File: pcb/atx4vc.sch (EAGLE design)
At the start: 69 parts, among them IC2 REG1117, IC3 STM32F042F4, IC4 MY_7905DT, J1 ATX24RH, SW1 324_SW, SW2 324_SW, SW3 324_SW, SW4 324_SW, SW5 324_SW, SW7 324_SW, U1 USBC_16P, U2 USBC_16P

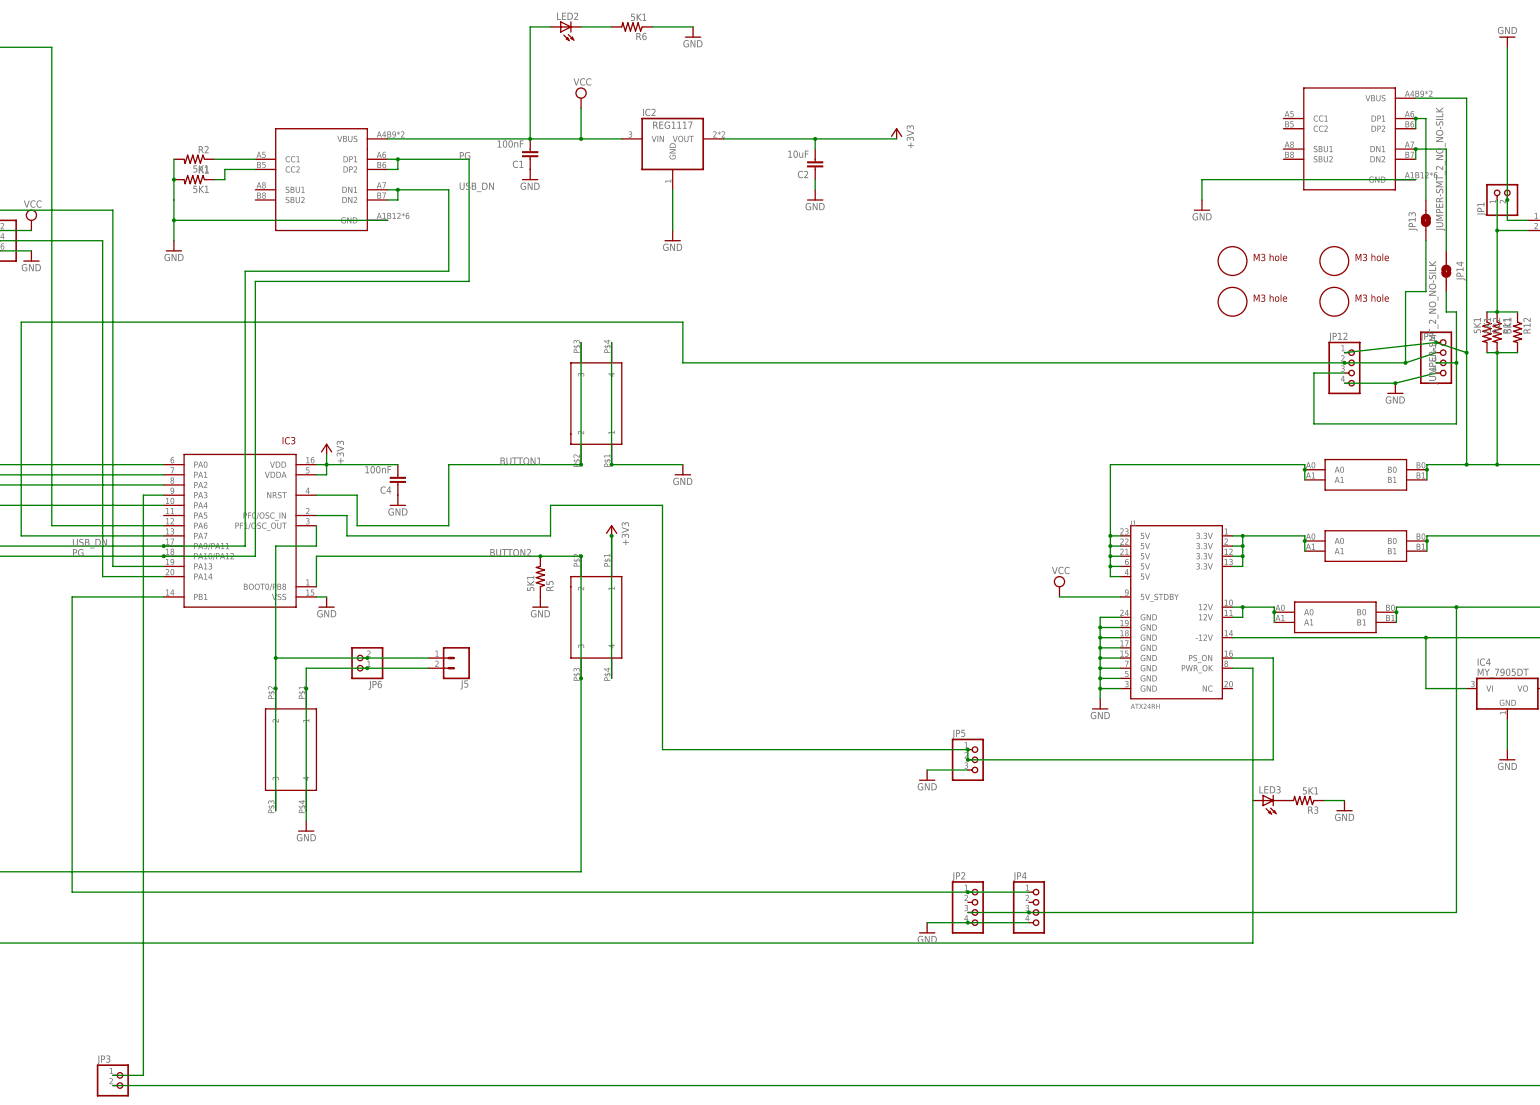
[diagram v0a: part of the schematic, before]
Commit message: adjusted ARGB header
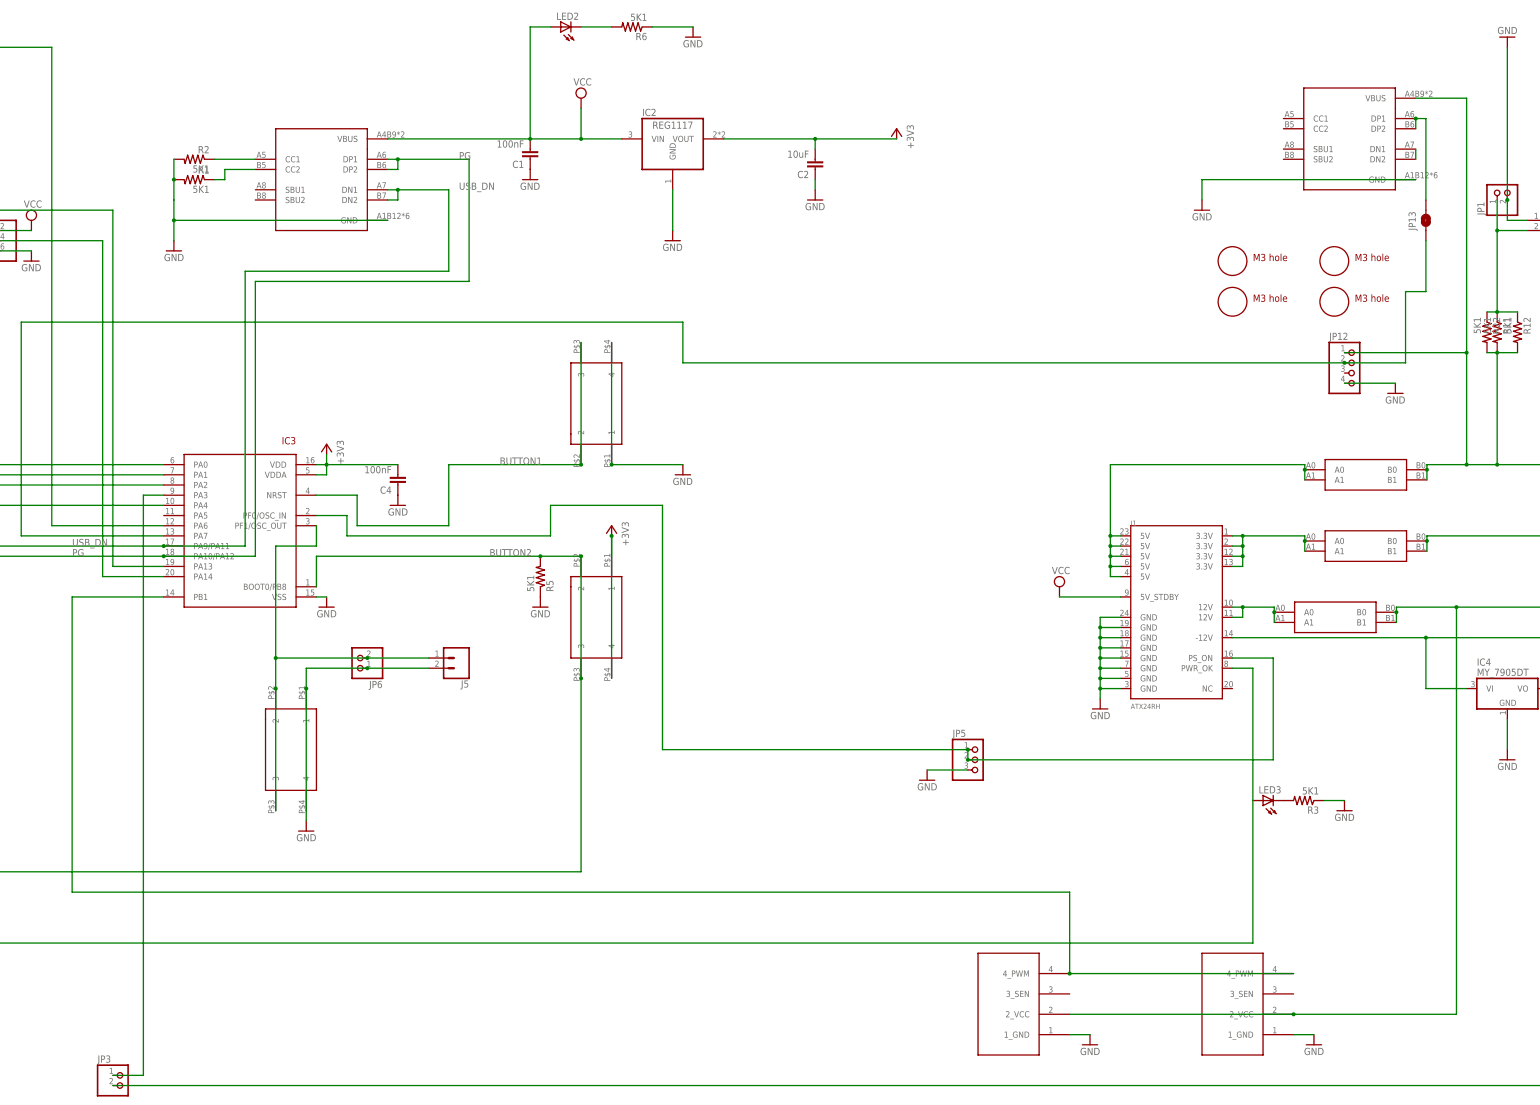
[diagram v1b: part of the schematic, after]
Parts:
- removed JP14: JUMPER-SMT_2_NO_NO-SILK, SparkFun-Jumpers:JUMPER-SMT_2_NO_NO-SILK
- removed JP2, JP4: (no value), atx_power_control:PINHD-1X4
- removed JP7: (no value), atx_power_control:PINHD-1X6
- added JP16, JP8: (no value), appleii:4PIN_FAN
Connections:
- removed net N$37: JP12.3, JP14.2, JP7.3
- net F12V: now also JP16.2_VCC, JP8.2_VCC; no longer JP2.3, JP4.3
- net F5V: no longer JP7.1
- net GND: now also JP16.1_GND, JP8.1_GND; no longer JP2.4, JP4.4, JP7.4
- net N$35: no longer JP7.2
- net N$36: no longer JP14.1
- net N$7: now also JP16.4_PWM, JP8.4_PWM; no longer JP2.1, JP4.1

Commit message: finishing touches
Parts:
- JP11: device atx_power_control:PINHD-1X3CB -> pinhead:PINHD-1X3
- JP12: device atx_power_control:PINHD-1X6 -> pinhead:PINHD-1X4
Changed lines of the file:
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@@
 <part name="U$7" library="atx_power_control" deviceset="CAR_FUSE_HOLDER" device="3IN1"/>
 <part name="U$8" library="atx_power_control" deviceset="CAR_FUSE_HOLDER" device="3IN1"/>
-<part name="JP12" library="atx_power_control" deviceset="PINHD-1X6" device=""/>
+<part name="JP12" library="pinhead" library_urn="urn:adsk.eagle:library:325" deviceset="PINHD-1X4" device="" package3d_urn="urn:adsk.eagle:package:22407/2"/>
 <part name="R14" library="atx_power_control" deviceset="RESISTOR" device="0805-RES" value="5K1"/>
-<part name="JP11" library="atx_power_control" deviceset="PINHD-1X3" device="CB"/>
+<part name="JP11" library="pinhead" library_urn="urn:adsk.eagle:library:325" deviceset="PINHD-1X3" device="" package3d_urn="urn:adsk.eagle:package:22458/2"/>
 <part name="SUPPLY1" library="supply2" library_urn="urn:adsk.eagle:library:372" deviceset="VCC" device=""/>
 <part name="GND34" library="supply1" deviceset="GND" device=""/>
@@
 <instance part="U$7" gate="G$1" x="281.94" y="20.32" smashed="yes"/>
 <instance part="U$8" gate="G$1" x="281.94" y="38.1" smashed="yes"/>
-<instance part="JP12" gate="A" x="279.4" y="60.96" smashed="yes">
-<attribute name="NAME" x="273.05" y="71.755" size="1.778" layer="95"/>
-<attribute name="VALUE" x="273.05" y="50.8" size="1.778" layer="96"/>
+<instance part="JP12" gate="A" x="279.4" y="63.5" smashed="yes">
+<attribute name="NAME" x="273.05" y="74.295" size="1.778" layer="95"/>
+<attribute name="VALUE" x="273.05" y="53.34" size="1.778" layer="96"/>
 </instance>
 <instance part="R14" gate="G$1" x="-86.36" y="149.86" smashed="yes" rot="R90">

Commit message: added 5VSB to terminal block, cleaned up files
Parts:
- removed C1, C4: 100nF, atx_power_control:CAP0805
- removed C2: 10uF, atx_power_control:CAP0805
- removed IC2: REG1117, atx_power_control:REG1117
- removed IC3: STM32F042F4, tx:STM32F042F4
- removed J5, J8: (no value), atx_power_control:CONN_023.5MM
- removed JP10: (no value), adafruit:PINHD-1X1CB
- removed JP11: (no value), pinhead:PINHD-1X3
- removed JP12: (no value), pinhead:PINHD-1X4
- removed JP13: JUMPER-SMT_2_NO_NO-SILK, SparkFun-Jumpers:JUMPER-SMT_2_NO_NO-SILK
- removed JP15: (no value), pinhead:PINHD-2X3
- removed JP16: (no value), appleii:4PIN_FAN
- removed JP5: (no value), atx_power_control:PINHD-1X3:1
- removed JP6: (no value), atx_power_control:PINHD-1X2
- removed JP9: (no value), atx_power_control:PINHD-2X4
- removed LED8: (no value), adafruit:LEDCHIP-LED0805
- removed R1, R14, R15, R18, R19, R2, R20, R21, R5: 5K1, atx_power_control:RESISTOR0805-RES
- removed SW1, SW2, SW3, SW4, SW5, SW7: 324_SW, 3pos_slide_switch_centered:324_SW
- removed U1, U2: USBC_16P, my_usbc_16p:USBC_16P
- added J4: (no value), SparkFun-Connectors:USB_C16PIN
- added JP2: (no value), pinhead:PINHD-1X2
- added JP4: (no value), pinhead:PINHD-2X2
- added U$11: M3_MOUNTING_HOLE, a:M3_MOUNTING_HOLE
- added U$12: PINHD1X4, adafruit_changed:PINHD1X4
- J1: device SparkFun-Connectors:ATX24RH -> nomcu:ATX24RH
- JP3: device pinhead:PINHD-1X2 -> pinhead:PINHD-2X3
- U$6: value 74LVC2G08 -> M3_MOUNTING_HOLE; device atx4vc:74LVC2G08 -> a:M3_MOUNTING_HOLE
- U$9: value WAGO257-7 -> DG2204R-5.0; device atx4vc:WAGO257-7 -> atx4vc:DG2204R-5.0
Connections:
- removed net +3V3: C2.2, C4.2, IC2.VOUT, IC3.VDD, IC3.VDDA, JP15.5, JP9.4, SW4.1, SW4.4, U$6.8_VCC
- removed net BUTTON1: IC3.NRST, SW3.2, SW3.3
- removed net BUTTON2: IC3.BOOT0/PB8, JP9.3, R5.2, SW4.2, SW4.3
- removed net F12V_DIV2: R18.2, R19.1, U$6.6_2B
- removed net N$12: U$6.2_1B, U$6.3_2Y
- removed net N$13: IC3.PA0, JP9.6, SW2.1, SW2.4
- removed net N$19: LED8.A, R15.2
- removed net N$22: IC3.PA1, JP9.8, SW5.1, SW5.4
- removed net N$23: IC3.PA2, JP10.1
- removed net N$24: JP3.2, U$6.7_1Y
- removed net N$25: IC3.PF0/OSC_IN, J1.PS_ON, JP5.1, JP5.2
- removed net N$26: IC3.PF1/OSC_OUT, J5.1, JP6.2, SW1.2, SW1.3
- removed net N$27: IC3.PA4, JP9.2, SW7.1, SW7.4
- removed net N$31: R1.1, U2.CC2
- removed net N$33: R2.1, U2.CC1
- removed net N$34: JP13.2, U1.DP1, U1.DP2
- removed net N$35: IC3.PA7, JP12.2, JP13.1
- removed net N$36: U1.DN1, U1.DN2
- removed net N$38: IC3.PA3, JP3.1
- removed net PG: IC3.PA10/PA12, J1.PWR_OK, JP15.1, LED3.A, U2.DP1, U2.DP2
- removed net USB_DN: IC3.PA9/PA11, R15.1, U2.DN1, U2.DN2
- new net N$11: J1.PWR_OK, JP3.5, LED3.A
- new net N$15: J1.PS_ON, JP2.2, JP3.6
- net -12V: now also U$9.P$7; no longer U$9.P$1
- net -5V: now also U$9.P$6; no longer U$9.P$2
- net F12V: now also U$4.P$5, U$9.P$3; no longer JP16.2_VCC, R18.1, U$4.P$7, U$9.P$7
- net F3V3: now also U$9.P$5; no longer R21.2, U$6.1_1A, U$9.P$3
- net F5V: now also J4.VBUS, U$12.1, U$4.P$4, U$9.P$4; no longer JP12.1, R20.1, U$4.P$5, U$6.5_2A, U$9.P$5, U1.VBUS
- net GND: now also J4.GND, J4.SHLD, JP2.1, JP3.2, U$12.4, U$9.P$2; no longer C1.1, C2.1, C4.1, IC2.GND, IC3.VSS, J5.2, J8.1, JP11.3, JP12.4, JP15.6, JP16.1_GND, JP5.3, JP6.1, JP9.1, JP9.5, JP9.7, LED8.C, R1.2, R19.2, R2.2, R20.2, R21.1, R5.1, SW1.1, SW1.4, SW2.2, SW2.3, SW3.1, SW3.4, SW5.2, SW5.3, SW7.2, SW7.3, U$4.P$4, U$6.4_GND, U$9.P$4, U$9.P$6, U1.GND, U2.GND
- net N$17: no longer J8.2
- net N$3: now also JP3.3, JP8.4_PWM; no longer IC3.PA14, JP15.4
- net N$4: now also J4.D+, JP4.2; no longer IC3.PA13, JP15.3
- net N$6: now also J4.D-, JP4.4; no longer IC3.PA6, JP11.1, R14.1
- net N$7: now also JP3.4, JP4.1, JP4.3, U$12.2; no longer IC3.PB1, JP16.4_PWM, JP8.4_PWM
- net VCC: now also JP3.1, U$4.P$7, U$9.P$1; no longer C1.2, IC2.VIN, JP11.2, JP15.2, R14.2, U2.VBUS
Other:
- moved on the sheet: R12

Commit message: finishing touches before production run
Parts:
- removed J4: (no value), SparkFun-Connectors:USB_C16PIN
- removed R11, R12: 5K1, atx_power_control:RESISTOR0805-RES
- added J2: ATX24RH, nomcu:ATX24RH
- added R1, R5: 5K1, atx_power_control:RESISTOR0805-RES
- C1: value 10uF -> 2.2uF
- J1: value ATX24RH -> (none); device nomcu:ATX24RH -> SparkFun-Connectors:USB_C16PIN
- JP1: device pinhead:PINHD-1X2 -> pinhead:PINHD-2X2
- JP4: device pinhead:PINHD-2X2 -> pinhead:PINHD-1X2
- R4, R7: device SparkFun-Passives:RESISTOR0805-RES -> atx_power_control:RESISTOR0805-RES
- R8, R9: device atx_power_control:RESISTOR0805-RES -> SparkFun-Passives:RESISTOR0805-RES
- U$10, U$11: value M3_MOUNTING_HOLE -> CAR_FUSE_HOLDER3IN1; device a:M3_MOUNTING_HOLE -> atx_power_control:CAR_FUSE_HOLDER3IN1
- U$12: value PINHD1X4 -> DG2204R-5.0; device adafruit_changed:PINHD1X4 -> atx4vc:DG2204R-5.0
- U$4: value VH396 -> M3_MOUNTING_HOLE; device 396_conn:VH396 -> a:M3_MOUNTING_HOLE
- U$5: value CAR_FUSE_HOLDER3IN1 -> M3_MOUNTING_HOLE; device atx_power_control:CAR_FUSE_HOLDER3IN1 -> a:M3_MOUNTING_HOLE
- U$7: value CAR_FUSE_HOLDER3IN1 -> VH396; device atx_power_control:CAR_FUSE_HOLDER3IN1 -> 396_conn:VH396
- U$8: value CAR_FUSE_HOLDER3IN1 -> PINHD1X4; device atx_power_control:CAR_FUSE_HOLDER3IN1 -> adafruit_changed:PINHD1X4
- U$9: value DG2204R-5.0 -> CAR_FUSE_HOLDER3IN1; device atx4vc:DG2204R-5.0 -> atx_power_control:CAR_FUSE_HOLDER3IN1
- renumbered C5 to C1, IC4 to IC1, JP8 to JP5, R22 to R2
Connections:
- removed net N$1 (its old number): LED3.C, R3.2
- removed net N$5 (its old number): LED1.C, R4.2
- new net N$18: LED3.C, R6.2
- new net N$20: LED2.C, R5.2
- net -12V: now also J2.-12V, R8.1, U$12.P$7, U$7.P$1; no longer J1.-12V, R7.1, U$4.P$1, U$9.P$7
- net -5V: now also R9.1, U$12.P$6, U$7.P$2; no longer R4.1, U$4.P$2, U$9.P$6
- net F12V: now also LED4.A, U$11.B0, U$11.B1, U$12.P$3, U$7.P$5; no longer LED5.A, U$4.P$5, U$5.B0, U$5.B1, U$9.P$3
- net F3V3: now also LED3.A, U$10.B0, U$10.B1, U$12.P$5, U$7.P$3; no longer LED6.A, U$4.P$3, U$7.B0, U$7.B1, U$9.P$5
- net F5V: now also J1.VBUS, LED2.A, R3.2, R4.2, U$12.P$4, U$7.P$4, U$8.1, U$9.B0, U$9.B1; no longer J4.VBUS, LED7.A, R11.2, R12.2, U$12.1, U$4.P$4, U$8.B0, U$8.B1, U$9.P$4
- net GND: now also J1.GND, J1.SHLD, J2.GND@0, J2.GND@1, J2.GND@2, J2.GND@3, J2.GND@4, J2.GND@5, J2.GND@6, J2.GND@7, JP2.2, JP4.1, LED5.A, LED6.A, R1.1, R5.1, R7.1, U$12.P$2, U$7.P$6, U$8.4; no longer J1.GND@0, J1.GND@1, J1.GND@2, J1.GND@3, J1.GND@4, J1.GND@5, J1.GND@6, J1.GND@7, J4.GND, J4.SHLD, JP1.2, JP2.1, LED1.A, LED4.A, R3.1, R8.1, R9.1, U$12.4, U$4.P$6, U$9.P$2
- net N$10: now also J2.5V@0, J2.5V@1, J2.5V@2, J2.5V@3, J2.5V@4, U$9.A0, U$9.A1; no longer J1.5V@0, J1.5V@1, J1.5V@2, J1.5V@3, J1.5V@4, U$8.A0, U$8.A1
- net N$11: now also J2.PWR_OK, LED7.A; no longer J1.PWR_OK, LED3.A
- net N$14: now also J2.3.3V@0, J2.3.3V@1, J2.3.3V@2, J2.3.3V@3, U$10.A0, U$10.A1; no longer J1.3.3V@0, J1.3.3V@1, J1.3.3V@2, J1.3.3V@3, U$7.A0, U$7.A1
- net N$15: now also J2.PS_ON, JP4.2; no longer J1.PS_ON, JP2.2
- net N$17: now also JP2.1, R3.1, R4.1; no longer JP1.1, R11.1, R12.1
- net N$21: now also J2.12V@0, J2.12V@1, U$11.A0, U$11.A1; no longer J1.12V@0, J1.12V@1, U$5.A0, U$5.A1
- net N$29: now also LED1.C, R1.2; no longer LED2.C, R6.2
- net N$4: now also J1.D+, JP1.2; no longer J4.D+, JP4.2
- net N$6: now also J1.D-, JP1.4; no longer J4.D-, JP4.4
- net N$7: now also JP1.1, JP1.3, U$8.2; no longer JP4.1, JP4.3, U$12.2
- net VCC: now also J2.5V_STDBY, LED1.A, U$12.P$1, U$7.P$7; no longer J1.5V_STDBY, LED2.A, U$4.P$7, U$9.P$1
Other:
- moved on the sheet: JP2, LED1, LED2, LED3, LED4, LED5, LED6, LED7, R10, R3, R4, R6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
